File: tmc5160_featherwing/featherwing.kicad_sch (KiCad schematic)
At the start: 2 parts, among them J3 Conn_01x16_P2.54MM_HeaderHoles, J4 Conn_01x12_P2.54MM_HeaderHoles

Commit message: Adjust connectors
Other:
- company: (none) -> Howard Hughes Medical Institute
- title: (none) -> tmc5160_featherwing
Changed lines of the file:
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@@
 (kicad_sch (version 20230121) (generator eeschema)
   (paper "A4")
+  (title_block
+    (title "tmc5160_featherwing")
+    (date "2024-04-04")
+    (rev "1.0")
+    (company "Howard Hughes Medical Institute")
+  )
   (symbol (lib_id "Janelia:Conn_01x16_P2.54MM_HeaderHoles") (at 74.93 90.17 0) (unit 1)
     (in_bom no) (on_board yes) (dnp no)

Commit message: Add to power sheet
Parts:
- renumbered J3 to J6, J4 to J7
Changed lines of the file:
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@@
   (title_block
     (title "tmc5160_featherwing")
-    (date "2024-04-04")
+    (date "2024-04-05")
     (rev "1.0")
     (company "Howard Hughes Medical Institute")
@@
   (symbol (lib_id "Janelia:Conn_01x16_P2.54MM_HeaderHoles") (at 74.93 90.17 0) (unit 1)
     (in_bom no) (on_board yes) (dnp no)
-    (property "Reference" "J3" (at 73.66 69.85 0)
+    (property "Reference" "J6" (at 73.66 69.85 0)
       (effects (font (size 1.27 1.27)))
     )
@@
       (project "tmc5160_featherwing"
         (path "/df2b2e89-e055-4140-95de-f1df723db034/69dff8eb-dcc1-4f17-9e1d-cf8103035e92"
-          (reference "J3") (unit 1)
+          (reference "J6") (unit 1)
         )
       )
@@
   (symbol (lib_id "Janelia:Conn_01x12_P2.54MM_HeaderHoles") (at 175.26 95.25 0) (unit 1)
     (in_bom no) (on_board yes) (dnp no)
-    (property "Reference" "J4" (at 173.99 80.01 0)
+    (property "Reference" "J7" (at 173.99 80.01 0)
       (effects (font (size 1.27 1.27)))
     )
@@
       (project "tmc5160_featherwing"
         (path "/df2b2e89-e055-4140-95de-f1df723db034/69dff8eb-dcc1-4f17-9e1d-cf8103035e92"
-          (reference "J4") (unit 1)
+          (reference "J7") (unit 1)
         )
       )

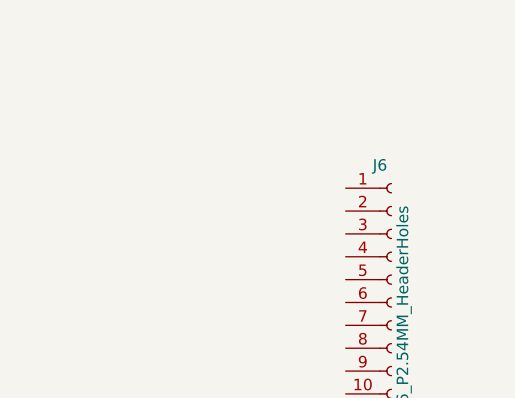
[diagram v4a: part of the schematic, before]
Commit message: Add capacitors and resistors
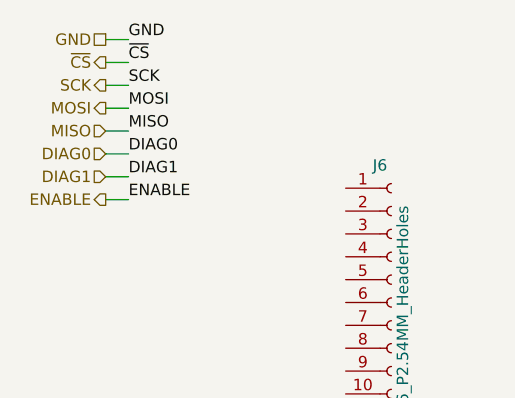
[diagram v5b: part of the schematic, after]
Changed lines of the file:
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@@
   (title_block
     (title "tmc5160_featherwing")
-    (date "2024-04-11")
+    (date "2024-04-12")
     (rev "1.0")
     (company "Howard Hughes Medical Institute")
   )
+  (wire (pts (xy 43.18 68.58) (xy 45.72 68.58))
+    (stroke (width 0) (type default))
+  )
+  (wire (pts (xy 43.18 71.12) (xy 45.72 71.12))
+    (stroke (width 0) (type default))
+  )
+  (wire (pts (xy 43.18 73.66) (xy 45.72 73.66))
+    (stroke (width 0) (type default))
+  )
+  (wire (pts (xy 43.18 63.5) (xy 45.72 63.5))
+    (stroke (width 0) (type default))
+  )
+  (wire (pts (xy 43.18 55.88) (xy 45.72 55.88))
+    (stroke (width 0) (type default))
+  )
+  (wire (pts (xy 43.18 60.96) (xy 45.72 60.96))
+    (stroke (width 0) (type default))
+  )
+  (wire (pts (xy 43.18 58.42) (xy 45.72 58.42))
+    (stroke (width 0) (type default))
+  )
+  (wire (pts (xy 43.18 66.04) (xy 45.72 66.04))
+    (stroke (width 0) (type default))
+  )
+  (label "~{CS}" (at 45.72 58.42 0) (fields_autoplaced)
+    (effects (font (size 1.27 1.27)) (justify left bottom))
+  )
+  (label "DIAG0" (at 45.72 68.58 0) (fields_autoplaced)
+    (effects (font (size 1.27 1.27)) (justify left bottom))
+  )
+  (label "MISO" (at 45.72 66.04 0) (fields_autoplaced)
+    (effects (font (size 1.27 1.27)) (justify left bottom))
+  )
+  (label "MOSI" (at 45.72 63.5 0) (fields_autoplaced)
+    (effects (font (size 1.27 1.27)) (justify left bottom))
+  )
+  (label "SCK" (at 45.72 60.96 0) (fields_autoplaced)
+    (effects (font (size 1.27 1.27)) (justify left bottom))
+  )
+  (label "ENABLE" (at 45.72 73.66 0) (fields_autoplaced)
+    (effects (font (size 1.27 1.27)) (justify left bottom))
+  )
+  (label "DIAG1" (at 45.72 71.12 0) (fields_autoplaced)
+    (effects (font (size 1.27 1.27)) (justify left bottom))
+  )
+  (label "GND" (at 45.72 55.88 0) (fields_autoplaced)
+    (effects (font (size 1.27 1.27)) (justify left bottom))
+  )
+  (hierarchical_label "GND" (shape passive) (at 43.18 55.88 180) (fields_autoplaced)
+    (effects (font (size 1.27 1.27)) (justify right))
+  )
+  (hierarchical_label "SCK" (shape output) (at 43.18 60.96 180) (fields_autoplaced)
+    (effects (font (size 1.27 1.27)) (justify right))
+  )
+  (hierarchical_label "ENABLE" (shape output) (at 43.18 73.66 180) (fields_autoplaced)
+    (effects (font (size 1.27 1.27)) (justify right))
+  )
+  (hierarchical_label "~{CS}" (shape output) (at 43.18 58.42 180) (fields_autoplaced)
+    (effects (font (size 1.27 1.27)) (justify right))
+  )
+  (hierarchical_label "DIAG0" (shape input) (at 43.18 68.58 180) (fields_autoplaced)
+    (effects (font (size 1.27 1.27)) (justify right))
+  )
+  (hierarchical_label "DIAG1" (shape input) (at 43.18 71.12 180) (fields_autoplaced)
+    (effects (font (size 1.27 1.27)) (justify right))
+  )
+  (hierarchical_label "MISO" (shape input) (at 43.18 66.04 180) (fields_autoplaced)
+    (effects (font (size 1.27 1.27)) (justify right))
+  )
+  (hierarchical_label "MOSI" (shape output) (at 43.18 63.5 180) (fields_autoplaced)
+    (effects (font (size 1.27 1.27)) (justify right))
+  )
   (symbol (lib_id "Janelia:Conn_01x16_P2.54MM_HeaderHoles") (at 74.93 90.17 0) (unit 1)

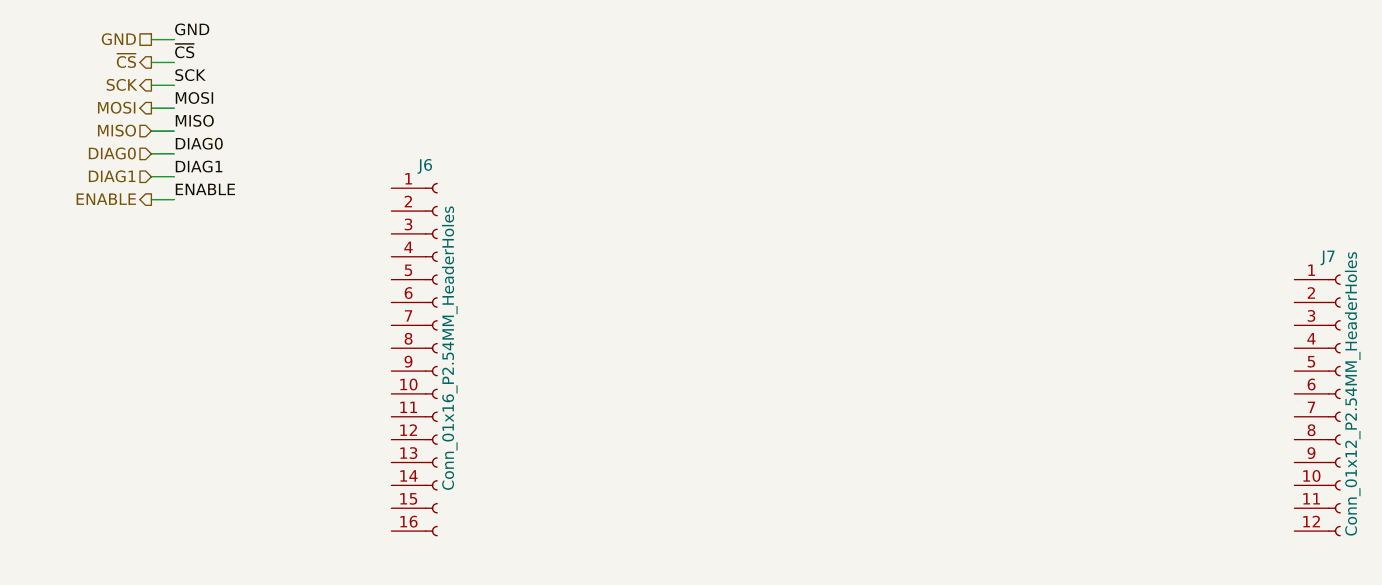
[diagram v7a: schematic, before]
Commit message: Add wires and labels
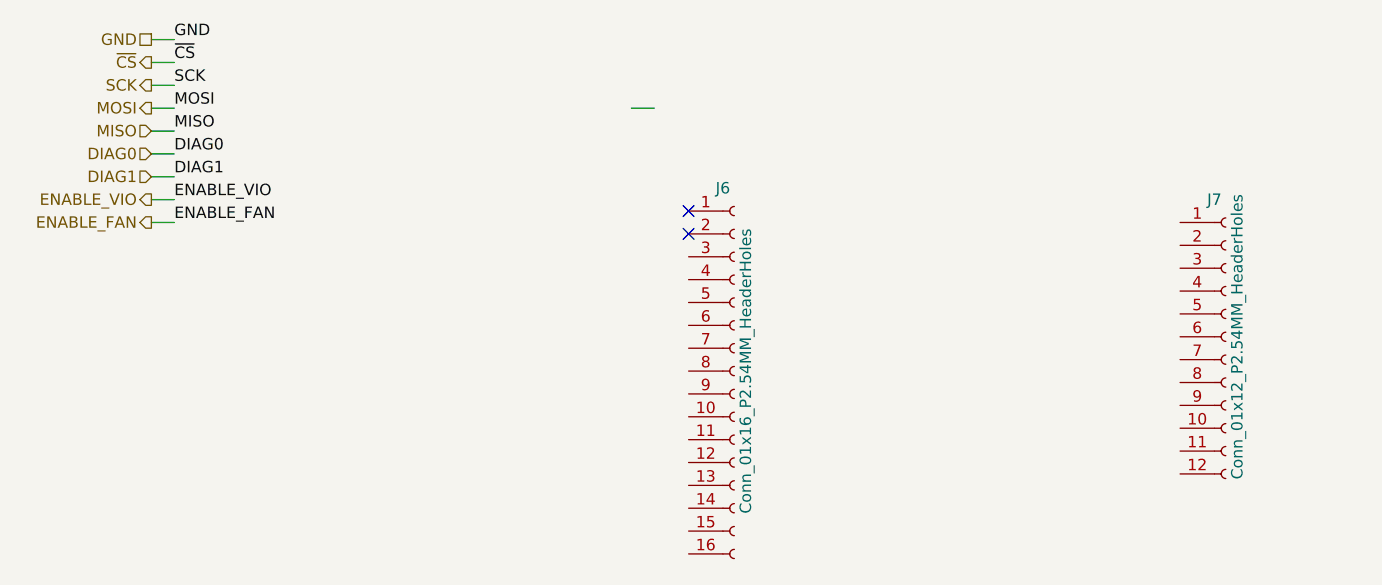
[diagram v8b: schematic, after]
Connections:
- no-connect marks 0 -> 2
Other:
- moved on the sheet: J6, J7
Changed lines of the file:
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@@
     (company "Howard Hughes Medical Institute")
+  )
+  (no_connect (at 102.87 74.93))
+  (no_connect (at 102.87 77.47))
+  (wire (pts (xy 43.18 76.2) (xy 45.72 76.2))
+    (stroke (width 0) (type default))
   )
   (wire (pts (xy 43.18 68.58) (xy 45.72 68.58))
@@
   )
   (wire (pts (xy 43.18 71.12) (xy 45.72 71.12))
-    (stroke (width 0) (type default))
-  )
-  (wire (pts (xy 43.18 73.66) (xy 45.72 73.66))
     (stroke (width 0) (type default))
   )
@@
     (stroke (width 0) (type default))
   )
+  (wire (pts (xy 96.52 63.5) (xy 99.06 63.5))
+    (stroke (width 0) (type default))
+  )
   (wire (pts (xy 43.18 58.42) (xy 45.72 58.42))
+    (stroke (width 0) (type default))
+  )
+  (wire (pts (xy 43.18 73.66) (xy 45.72 73.66))
     (stroke (width 0) (type default))
   )
@@
     (effects (font (size 1.27 1.27)) (justify left bottom))
   )
+  (label "ENABLE_FAN" (at 45.72 76.2 0) (fields_autoplaced)
+    (effects (font (size 1.27 1.27)) (justify left bottom))
+  )
   (label "DIAG0" (at 45.72 68.58 0) (fields_autoplaced)
+    (effects (font (size 1.27 1.27)) (justify left bottom))
+  )
+  (label "ENABLE_VIO" (at 45.72 73.66 0) (fields_autoplaced)
     (effects (font (size 1.27 1.27)) (justify left bottom))
   )
@@
   )
   (label "SCK" (at 45.72 60.96 0) (fields_autoplaced)
-    (effects (font (size 1.27 1.27)) (justify left bottom))
-  )
-  (label "ENABLE" (at 45.72 73.66 0) (fields_autoplaced)
     (effects (font (size 1.27 1.27)) (justify left bottom))
   )
@@
     (effects (font (size 1.27 1.27)) (justify right))
   )
-  (hierarchical_label "ENABLE" (shape output) (at 43.18 73.66 180) (fields_autoplaced)
+  (hierarchical_label "ENABLE_VIO" (shape output) (at 43.18 73.66 180) (fields_autoplaced)
+    (effects (font (size 1.27 1.27)) (justify right))
+  )
+  (hierarchical_label "ENABLE_FAN" (shape output) (at 43.18 76.2 180) (fields_autoplaced)
     (effects (font (size 1.27 1.27)) (justify right))
   )
@@
     (effects (font (size 1.27 1.27)) (justify right))
   )
-  (symbol (lib_id "Janelia:Conn_01x16_P2.54MM_HeaderHoles") (at 74.93 90.17 0) (unit 1)
+  (symbol (lib_id "Janelia:Conn_01x16_P2.54MM_HeaderHoles") (at 107.95 92.71 0) (unit 1)
     (in_bom no) (on_board yes) (dnp no)
-    (property "Reference" "J6" (at 73.66 69.85 0)
+    (property "Reference" "J6" (at 106.68 72.39 0)
       (effects (font (size 1.27 1.27)))
     )
-    (property "Value" "Conn_01x16_P2.54MM_HeaderHoles" (at 76.2 90.17 90)
+    (property "Value" "Conn_01x16_P2.54MM_HeaderHoles" (at 109.22 92.71 90)
       (effects (font (size 1.27 1.27)))
     )
-    (property "Footprint" "Janelia:PinHeader_1x16_P2.54mm_Vertical_Holes" (at 74.93 90.17 0)
+    (property "Footprint" "Janelia:PinHeader_1x16_P2.54mm_Vertical_Holes" (at 107.95 92.71 0)
       (effects (font (size 1.27 1.27)) hide)
     )
-    (property "Datasheet" "~" (at 74.93 90.17 0)
+    (property "Datasheet" "~" (at 107.95 92.71 0)
       (effects (font (size 1.27 1.27)) hide)
     )
@@
     )
   )
-  (symbol (lib_id "Janelia:Conn_01x12_P2.54MM_HeaderHoles") (at 175.26 95.25 0) (unit 1)
+  (symbol (lib_id "Janelia:Conn_01x12_P2.54MM_HeaderHoles") (at 162.56 88.9 0) (unit 1)
     (in_bom no) (on_board yes) (dnp no)
-    (property "Reference" "J7" (at 173.99 80.01 0)
+    (property "Reference" "J7" (at 161.29 73.66 0)
       (effects (font (size 1.27 1.27)))
     )
-    (property "Value" "Conn_01x12_P2.54MM_HeaderHoles" (at 176.53 95.25 90)
+    (property "Value" "Conn_01x12_P2.54MM_HeaderHoles" (at 163.83 88.9 90)
       (effects (font (size 1.27 1.27)))
     )
-    (property "Footprint" "Janelia:PinHeader_1x12_P2.54mm_Vertical_Holes" (at 175.26 95.25 0)
+    (property "Footprint" "Janelia:PinHeader_1x12_P2.54mm_Vertical_Holes" (at 162.56 88.9 0)
       (effects (font (size 1.27 1.27)) hide)
     )
-    (property "Datasheet" "~" (at 175.26 95.25 0)
+    (property "Datasheet" "~" (at 162.56 88.9 0)
       (effects (font (size 1.27 1.27)) hide)
     )
